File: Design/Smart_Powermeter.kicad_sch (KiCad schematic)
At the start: 43 parts, among them Q1 LBSS84LT1G, U1 TYPE-C_16PIN_2MD(073), U2 ESP32-S2-MINI-2-N4R2, U3 AMS1117-3.3, U4 FPC-05FB-24PH20

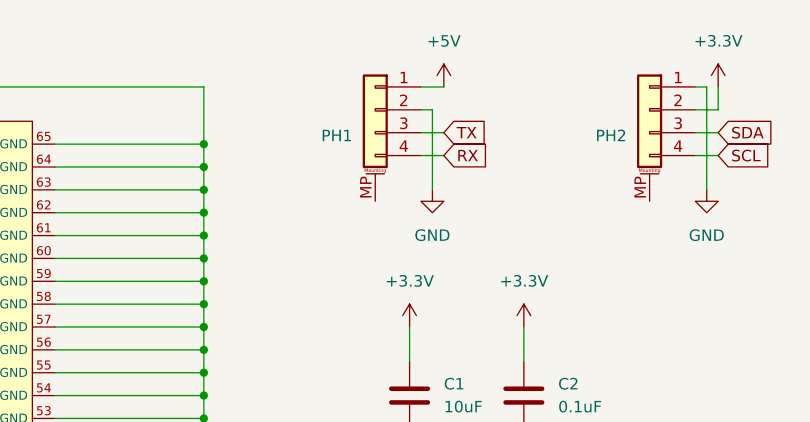
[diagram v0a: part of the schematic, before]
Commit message: Cleared path around antenna and removed Serial port
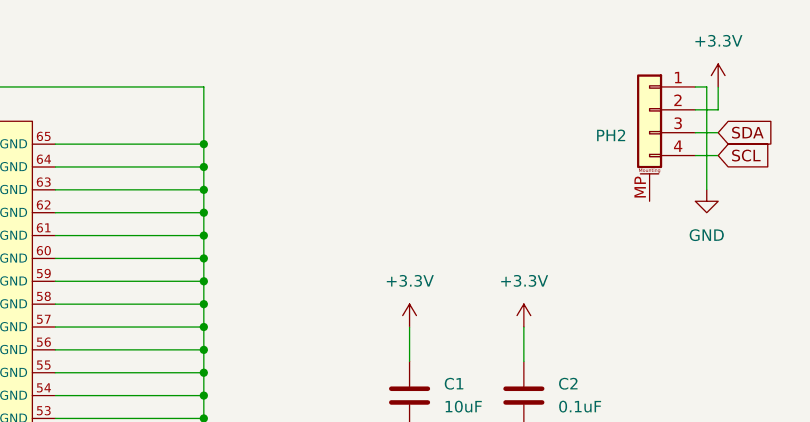
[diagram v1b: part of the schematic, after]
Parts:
- removed PH1: Conn_01x04_MountingPin, Connector_PinHeader_2.54mm:PinHeader_1x04_P2.54mm_Vertical, symbol Connector_Generic_MountingPin:Conn_01x04_MountingPin
